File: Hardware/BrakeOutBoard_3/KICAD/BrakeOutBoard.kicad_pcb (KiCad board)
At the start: 2 copper layers, 63 x 80 mm, 69 parts, among them J20 Conn_01x19_Socket, J5 Conn_01x19_Socket, K15 K15, K30 K30, K31 K31, K501 K31, K502 K31, K503 K31, K504 K31, Q1 MMDT3904, Q2 LBSS84LT1G, U1 LTV-847, U101 SN65HVD230DR, U2 LTV-847, U3 LVT 817, U4 LTV-847, U501 MCP23017_ML

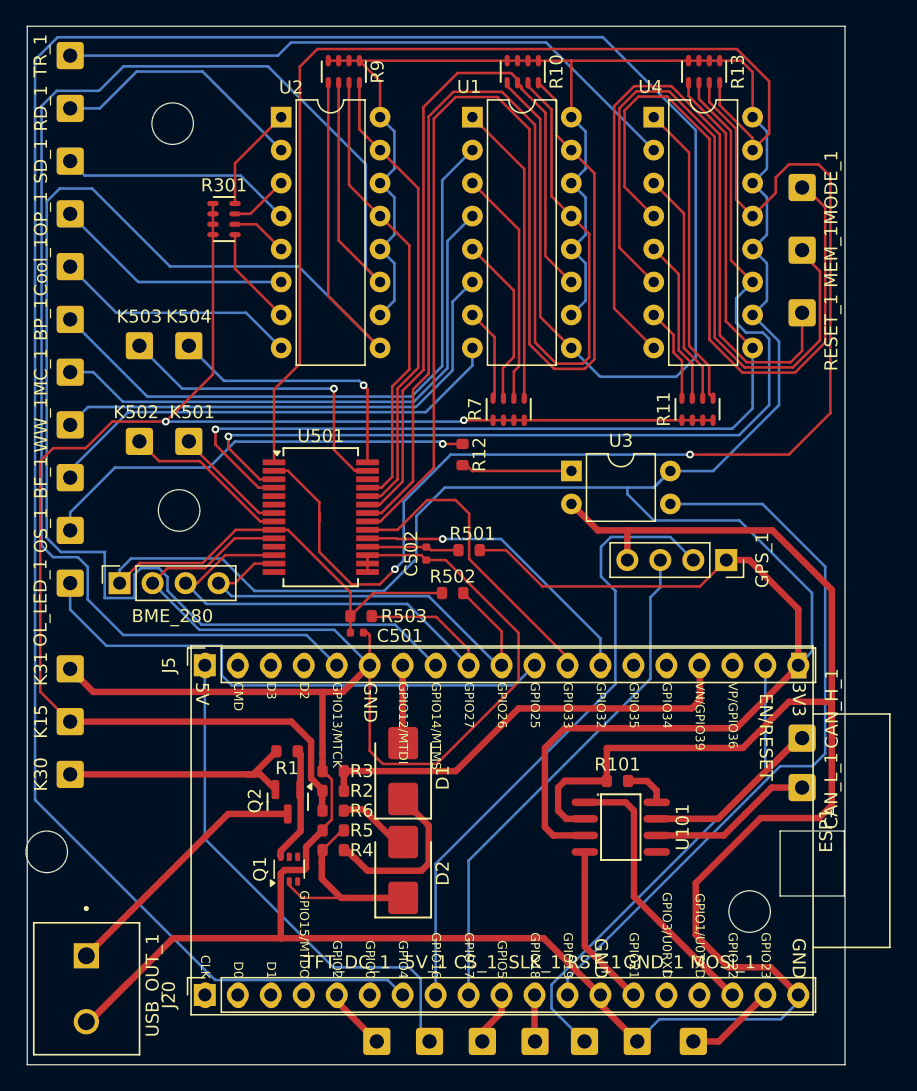
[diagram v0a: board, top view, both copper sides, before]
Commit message: Add files via upload
Board didn#t fit, now it is 1 mm lower
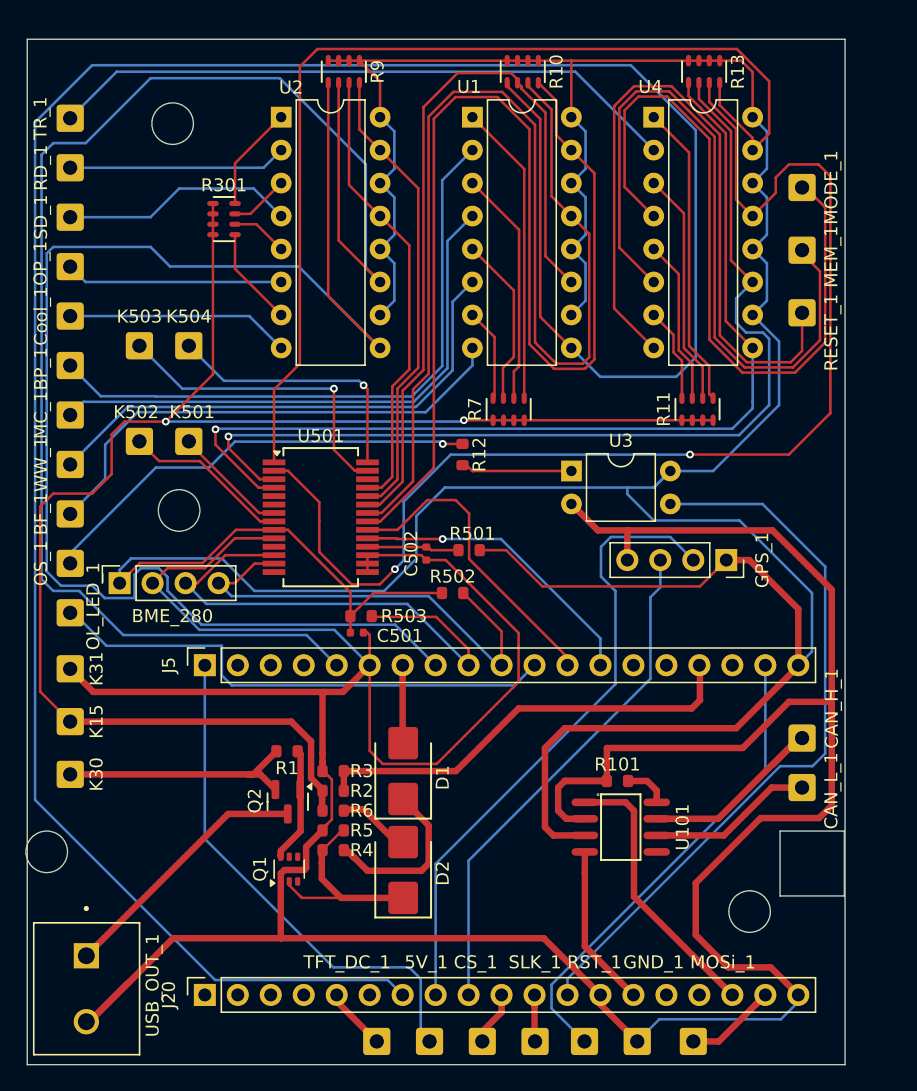
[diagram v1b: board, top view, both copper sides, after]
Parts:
- removed ESP1: ~, PCM_Espressif:ESP32-DevKitC
- moved TR_1 4.83 mm to (127.3, 81.7)
- moved RD_1 4.57 mm to (127.3, 85.5)
- moved SD_1 4.32 mm to (127.3, 89.3)
- moved OP_1 4.06 mm to (127.3, 93.1)
- moved Cool_1 3.81 mm to (127.3, 96.9)
- moved BP_1 3.56 mm to (127.3, 100.7)
- moved MC_1 3.30 mm to (127.3, 104.5)
- moved WW_1 3.05 mm to (127.3, 108.4)
- moved BF_1 2.79 mm to (127.3, 112.2)
- moved OS_1 2.54 mm to (127.3, 116.0)
- moved OL_LED_1 2.29 mm to (127.3, 119.8)
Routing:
- net GPIO 14 (PIN 12): track 118.6 -> 112.0 mm
- net GPIO 4 (PIN 26): track 197.2 -> 192.6 mm
- net /Optocopler/DoorRight: track 19.9 -> 16.8 mm
- net GPIO 13 (PIN 15): track 117.1 -> 114.2 mm
- net Net-(BF_1-Pin_1): track 36.3 -> 38.6 mm
- net Net-(J5-Pin_11): track 42.2 -> 40.2 mm
- net /Optocopler/OilPresure: track 18.4 -> 16.7 mm
- net /Optocopler/Coolant: track 18.9 -> 17.3 mm
- net /Optocopler/BrakePads: track 49.7 -> 48.2 mm
- net Net-(OS_1-Pin_1): track 33.2 -> 34.6 mm
- net /Optocopler/WhiperWater: track 38.6 -> 39.9 mm
- net PortExpander GPB1: track 96.0 -> 95.4 mm
- net /Optocopler/MotorCap: track 43.6 -> 43.1 mm
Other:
- board size 63 x 80 mm -> 63 x 79 mm
